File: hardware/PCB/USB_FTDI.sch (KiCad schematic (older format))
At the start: 10 parts, among them J1 USB_B_Micro, U2 FT230XQ

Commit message: corretcted usb plus minus connection
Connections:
- net labels added: USB_D_M, USB_D_P
- wire segments 46 -> 48
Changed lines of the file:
@@
 	7650 3200 7650 3100
 Wire Wire Line
-	2700 4100 5200 4100
+	3050 4100 2700 4100
 Wire Wire Line
-	2700 4200 5200 4200
+	3050 4200 2700 4200
+Text Label 2750 4100 0    50   ~ 0
+USB_D_P
+Text Label 2750 4200 0    50   ~ 0
+USB_D_M
+Wire Wire Line
+	4350 4100 5200 4100
+Wire Wire Line
+	4350 4200 5200 4200
+Text Label 4350 4100 0    50   ~ 0
+USB_D_M
+Text Label 4350 4200 0    50   ~ 0
+USB_D_P
 $EndSCHEMATC

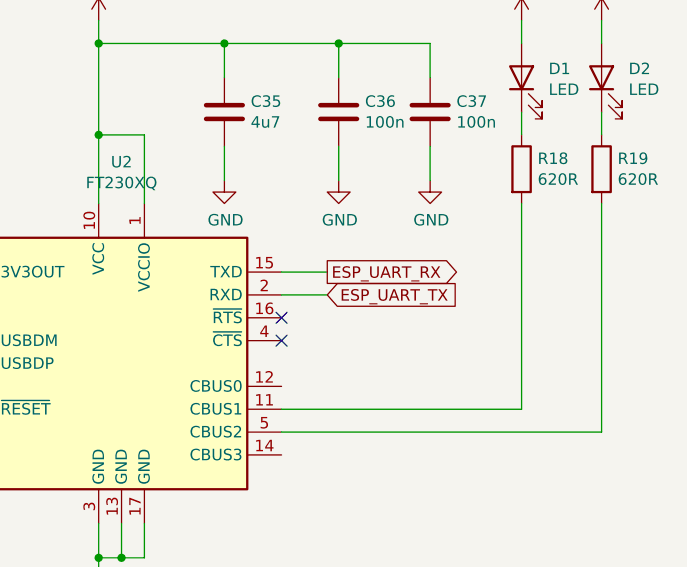
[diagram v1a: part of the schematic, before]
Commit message: add 32khz crystal for rtc
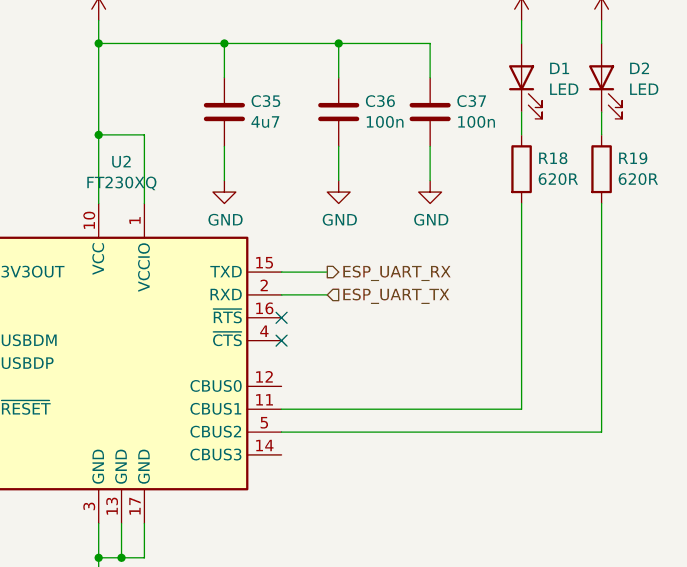
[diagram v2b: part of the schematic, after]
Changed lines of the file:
@@
 NoConn ~ 6600 4000
 NoConn ~ 6600 4100
-Text GLabel 6800 3800 2    50   Output ~ 0
-ESP_UART_RX
-Wire Wire Line
-	6600 3800 6800 3800
-Text GLabel 6800 3900 2    50   Input ~ 0
-ESP_UART_TX
 Wire Wire Line
 	6800 3900 6600 3900
@@
 Text Label 4350 4200 0    50   ~ 0
 USB_D_P
+Text HLabel 6800 3800 2    50   Output ~ 0
+ESP_UART_RX
+Wire Wire Line
+	6600 3800 6800 3800
+Text HLabel 6800 3900 2    50   Input ~ 0
+ESP_UART_TX
 $EndSCHEMATC

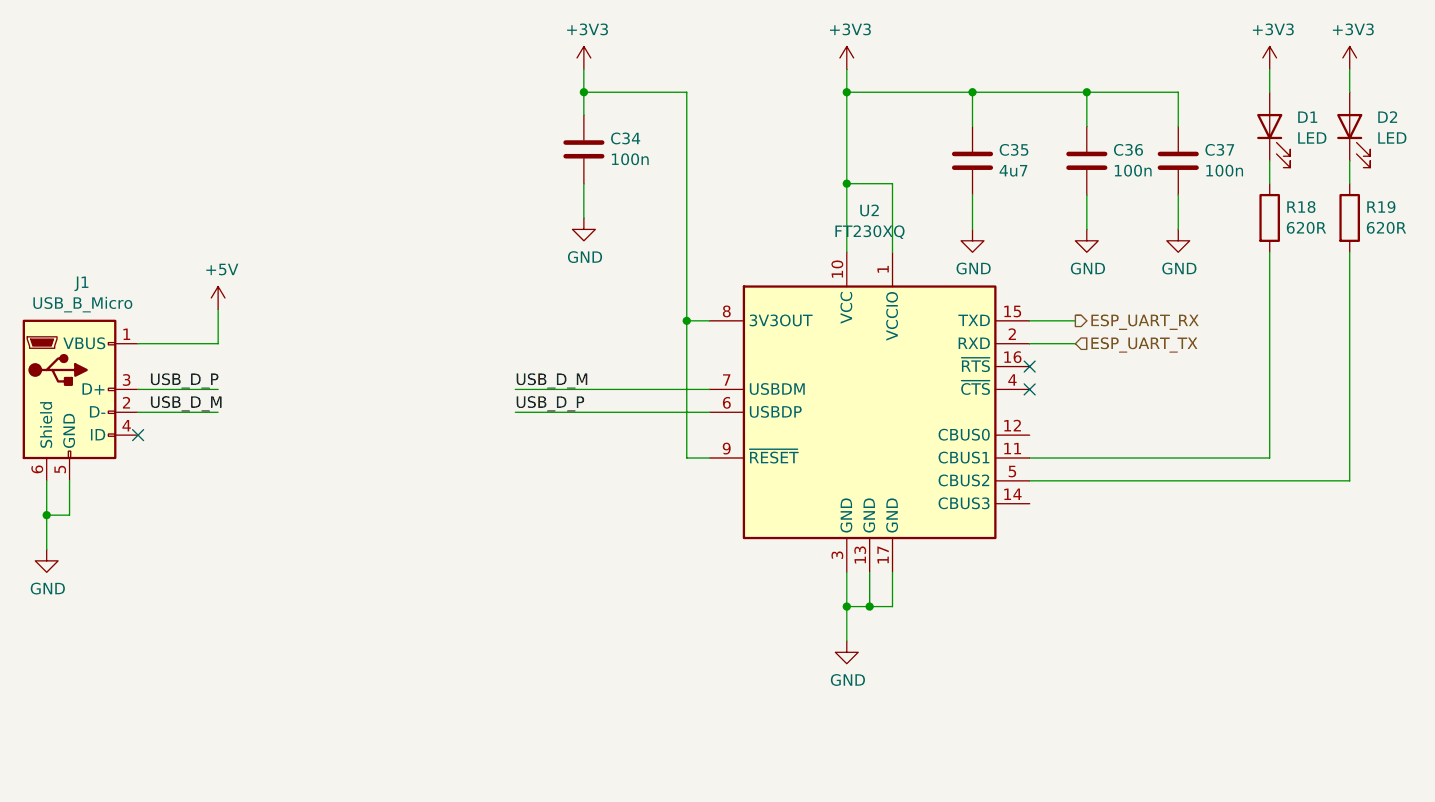
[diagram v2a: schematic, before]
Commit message: changed FTDI chip to full handshake chip
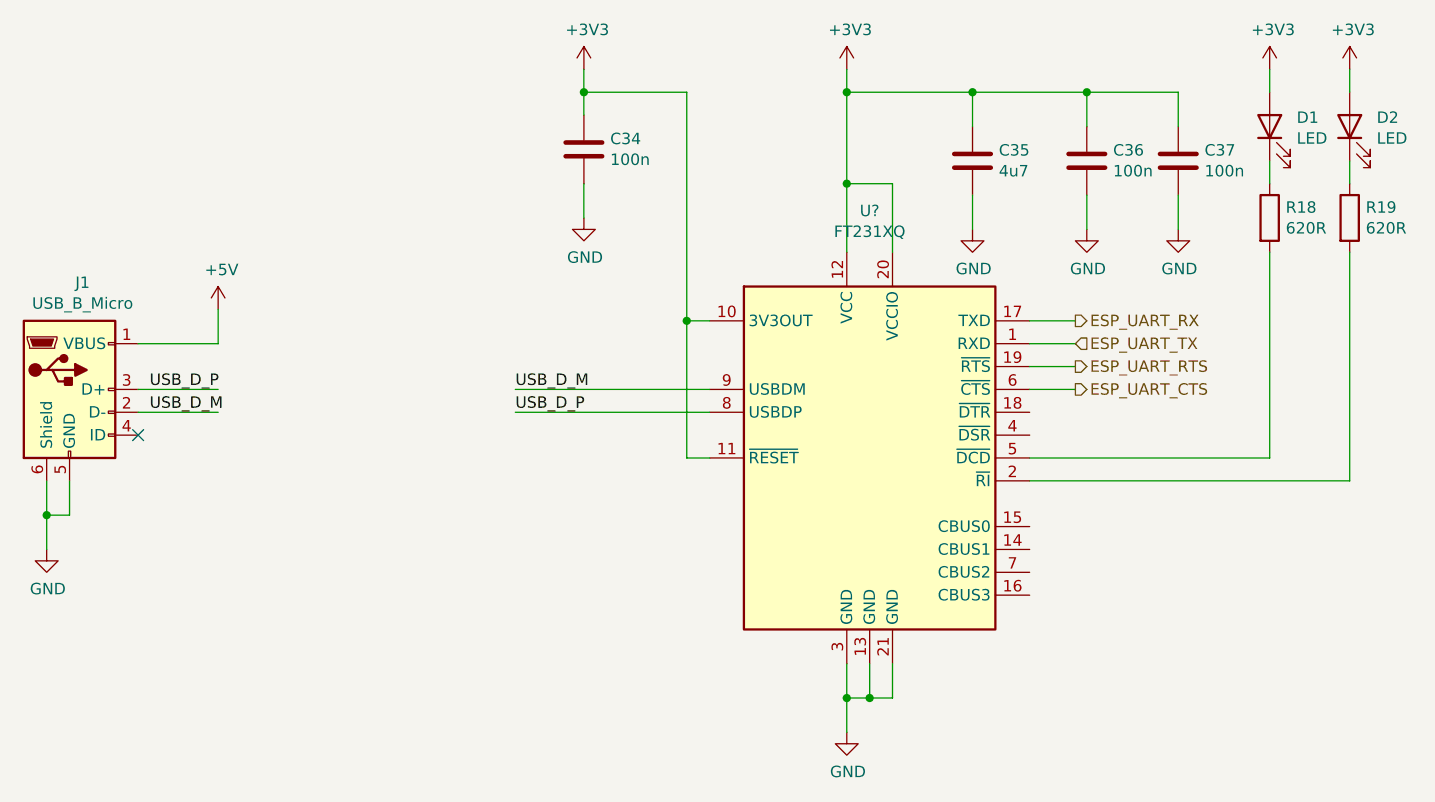
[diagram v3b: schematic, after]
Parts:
- removed U2: FT230XQ, Package_DFN_QFN:QFN-16-1EP_4x4mm_P0.65mm_EP2.1x2.1mm, symbol Interface_USB:FT230XQ
- added U?: FT231XQ, Package_DFN_QFN:QFN-20-1EP_4x4mm_P0.5mm_EP2.5x2.5mm, symbol Interface_USB:FT231XQ
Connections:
- net labels added: ESP_UART_CTS, ESP_UART_RTS
- wire segments 48 -> 50
- no-connect marks 3 -> 1
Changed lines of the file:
@@
 NoConn ~ 2700 4300
-$Comp
-L Interface_USB:FT230XQ U?
-U 1 1 5FE9F19A
-P 5900 4200
-AR Path="/5FE9F19A" Ref="U?"  Part="1"
-AR Path="/5FE9624E/5FE9F19A" Ref="U2"  Part="1"
-F 0 "U2" H 5900 5081 50  0000 C CNN
-F 1 "FT230XQ" H 5900 4990 50  0000 C CNN
-F 2 "Package_DFN_QFN:QFN-16-1EP_4x4mm_P0.65mm_EP2.1x2.1mm" H 7250 3600 50  0001 C CNN
-F 3 "https://www.ftdichip.com/Support/Documents/DataSheets/ICs/DS_FT230X.pdf" H 5900 4200 50  0001 C CNN
-	1    5900 4200
-	1    0    0    -1
-$EndComp
 $Comp
 L Device:C C?
@@
 L power:GND #PWR?
 U 1 1 5FE9F1FC
-P 5800 5200
+P 5800 5600
 AR Path="/5FE9F1FC" Ref="#PWR?"  Part="1"
 AR Path="/5FE9624E/5FE9F1FC" Ref="#PWR082"  Part="1"
-F 0 "#PWR082" H 5800 4950 50  0001 C CNN
-F 1 "GND" H 5805 5027 50  0000 C CNN
-F 2 "" H 5800 5200 50  0001 C CNN
-F 3 "" H 5800 5200 50  0001 C CNN
-	1    5800 5200
-	1    0    0    -1
-$EndComp
-Wire Wire Line
-	5800 4900 5800 5050
-Wire Wire Line
-	5900 5050 5800 5050
-Connection ~ 5800 5050
-Wire Wire Line
-	5800 5050 5800 5200
-Wire Wire Line
-	5900 4900 5900 5050
-Wire Wire Line
-	6000 4900 6000 5050
-Wire Wire Line
-	6000 5050 5900 5050
-Connection ~ 5900 5050
-NoConn ~ 6600 4000
-NoConn ~ 6600 4100
+F 0 "#PWR082" H 5800 5350 50  0001 C CNN
+F 1 "GND" H 5805 5427 50  0000 C CNN
+F 2 "" H 5800 5600 50  0001 C CNN
+F 3 "" H 5800 5600 50  0001 C CNN
+	1    5800 5600
+	1    0    0    -1
+$EndComp
+Wire Wire Line
+	5800 5300 5800 5450
+Wire Wire Line
+	5900 5450 5800 5450
+Connection ~ 5800 5450
+Wire Wire Line
+	5800 5450 5800 5600
+Wire Wire Line
+	5900 5300 5900 5450
 Wire Wire Line
 	6800 3900 6600 3900
@@
 Text HLabel 6800 3900 2    50   Input ~ 0
 ESP_UART_TX
+Wire Wire Line
+	5900 5450 6000 5450
+Wire Wire Line
+	6000 5450 6000 5300
+Connection ~ 5900 5450
+Text HLabel 6800 4000 2    50   Output ~ 0
+ESP_UART_RTS
+Text HLabel 6800 4100 2    50   Output ~ 0
+ESP_UART_CTS
+$Comp
+L Interface_USB:FT231XQ U?
+U 1 1 5FFEC088
+P 5900 4400
+F 0 "U?" H 5900 5481 50  0000 C CNN
+F 1 "FT231XQ" H 5900 5390 50  0000 C CNN
+F 2 "Package_DFN_QFN:QFN-20-1EP_4x4mm_P0.5mm_EP2.5x2.5mm" H 7250 3600 50  0001 C CNN
+F 3 "https://www.ftdichip.com/Support/Documents/DataSheets/ICs/DS_FT231X.pdf" H 5900 4400 50  0001 C CNN
+	1    5900 4400
+	1    0    0    -1
+$EndComp
+Wire Wire Line
+	6600 4000 6800 4000
+Wire Wire Line
+	6600 4100 6800 4100
 $EndSCHEMATC

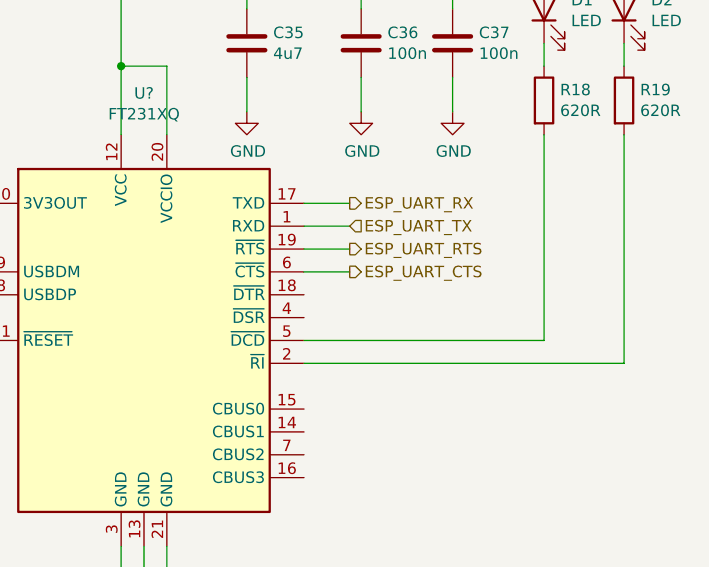
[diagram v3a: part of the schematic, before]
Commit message: changed to dtr
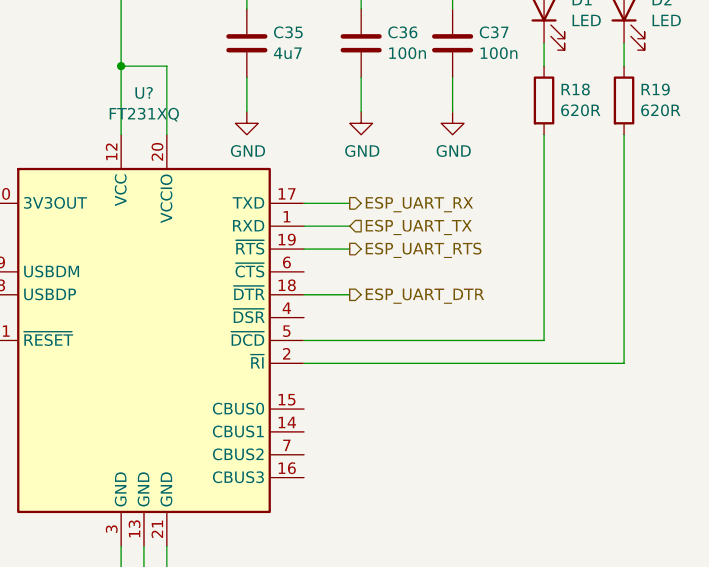
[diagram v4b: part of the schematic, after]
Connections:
- net labels added: ESP_UART_DTR
- net labels removed: ESP_UART_CTS
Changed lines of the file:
@@
 Text HLabel 6800 4000 2    50   Output ~ 0
 ESP_UART_RTS
-Text HLabel 6800 4100 2    50   Output ~ 0
-ESP_UART_CTS
+Text HLabel 6800 4200 2    50   Output ~ 0
+ESP_UART_DTR
 $Comp
 L Interface_USB:FT231XQ U?
@@
 	6600 4000 6800 4000
 Wire Wire Line
-	6600 4100 6800 4100
+	6600 4200 6800 4200
 $EndSCHEMATC

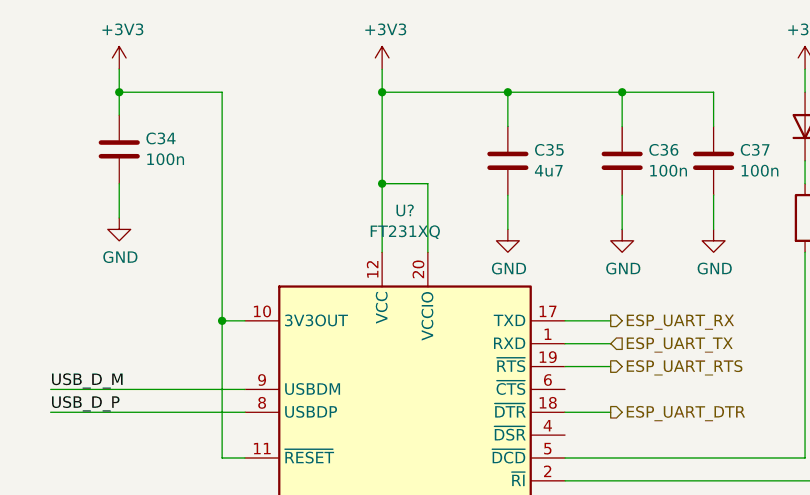
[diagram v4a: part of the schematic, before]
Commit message: add enable and boot0 buttons
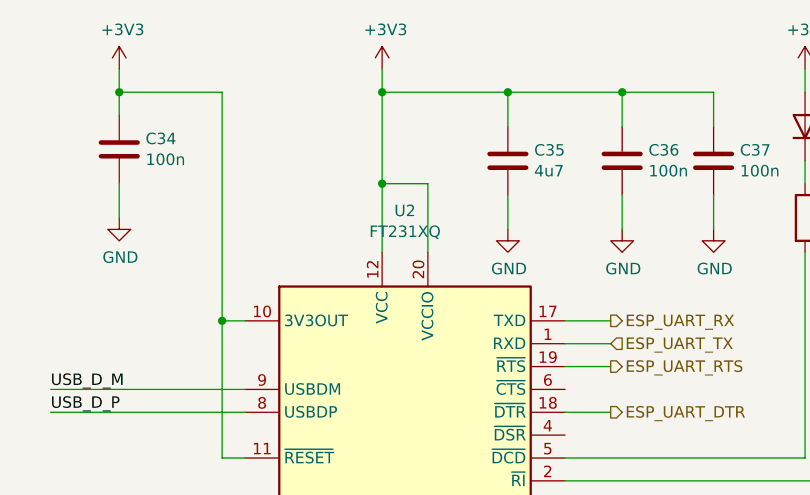
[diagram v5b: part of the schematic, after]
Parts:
- gave numbers to parts that had none: 1
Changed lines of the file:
@@
 ESP_UART_DTR
 $Comp
-L Interface_USB:FT231XQ U?
+L Interface_USB:FT231XQ U2
 U 1 1 5FFEC088
 P 5900 4400
-F 0 "U?" H 5900 5481 50  0000 C CNN
+F 0 "U2" H 5900 5481 50  0000 C CNN
 F 1 "FT231XQ" H 5900 5390 50  0000 C CNN
 F 2 "Package_DFN_QFN:QFN-20-1EP_4x4mm_P0.5mm_EP2.5x2.5mm" H 7250 3600 50  0001 C CNN
